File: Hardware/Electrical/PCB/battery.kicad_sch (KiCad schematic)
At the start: 0 parts

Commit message: battery charger added
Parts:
- added BT1, BT2, BT3, BT4: Li-ion 3.3Ah, symbol Device:Battery_Cell
- added C16, C18, C26: 1u, symbol Device:C_Small
- added C17: 2.2u, symbol Device:C_Small
- added C19, C20, C21: 0.1u, symbol Device:C_Small
- added C22: 22p, symbol Device:C_Small
- added C23, C24: 10u, symbol Device:C
- added C25: 100n, symbol Device:C
- added D3: BAT43W-V, Diode_SMD:D_SOD-123, symbol Diode:BAT43W-V
- added D4: SS34, Diode_SMD:D_SMC, symbol Diode:SS34
- added J2: jst, symbol Connector_Generic:Conn_01x02
- added L2: L, symbol Device:L
- added Q1, Q2: DMT6008LFG-7, Package_SON:Diodes_PowerDI3333-8, symbol Transistor_FET:DMT6008LFG
- added R10: 10m, symbol Device:R_Small
- added R11: 931k, symbol Device:R
- added R12: 133k, symbol Device:R
- added R13, R14: 10k, symbol Device:R
- added R15: 5.1k, symbol Device:R
- added R16: 430k, symbol Device:R
- added R17: 115k, symbol Device:R
- added R18: 25.5k, symbol Device:R
- added R8: 10, symbol Device:R_Small
- added R9: 2k, symbol Device:R_Small
- added U6: BQ24600, Package_DFN_QFN:Texas_RVA_VQFN-16-1EP_3.5x3.5mm_P0.5mm_EP2.14x2.14mm_ThermalVias, symbol Battery_Management:BQ24650
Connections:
- new net: BT4.1 (+), C20.2, C22.2, C23.1, C24.1, C25.1, R10.2, R11.1, U6.9 (SRN)
- new net: BT3.1 (+), BT4.2 (-)
- new net: Q1.4 (G), U6.13 (LODRV)
- new net: C19.2, L2.1, Q1.5 (D), Q2.1 (S), Q2.2 (S), Q2.3 (S), U6.14 (PH)
- new net: C20.1, C21.2, L2.2, R10.1, U6.10 (SRP)
- new net: C17.1, R9.2
- new net: BT1.1 (+), BT2.2 (-)
- new net: C22.1, R11.2, R12.1, U6.8 (VFB)
- new net: BT2.1 (+), BT3.2 (-)
- new net: C19.1, D3.1 (K), U6.16 (BTST)
- new net: C18.1, D3.2 (A), U6.12 (REGN)
- new net: C16.1, R8.2, U6.1 (VCC)
- new net: Q2.4 (G), U6.15 (HIDRV)
- new net: D4.1 (K), Q2.5 (D), R8.1
- new net +3.3V: R13.1, R14.1
- new net CHARGE_EN: U6.2 (CE)
- new net GND: BT1.2 (-), C16.2, C17.2, C18.2, C21.1, C23.2, C24.2, C25.2, C26.2, J2.2 (Pin_2), Q1.1 (S), Q1.2 (S), Q1.3 (S), R12.2, R16.2, R18.2, U6.11 (GND), U6.17 (GND)
- new net ISET_BT: R17.2, R18.1, U6.7 (ISET)
- new net PD_PWR: D4.2 (A), R9.1
- new net PG_BT: R14.2, U6.5 (PG)
- new net STATUS_BT: R13.2, U6.3 (STAT1)
- new net TEMPSNS_BT: J2.1 (Pin_1), R15.2, R16.1, U6.4 (TS)
- new net VREF_BT: C26.1, R15.1, R17.1, U6.6 (VREF)
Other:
- note added: "10k NTC"
- note added: "From USBC PD"
- note added: "To uC"
- note added: "Unclear if Working Change Values in Testing Maybe disable Later"
- note added: "VREF 2.1V VSET 4*4.2V=16.8V"
- note added: "set to 55°C"

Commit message: project state at start of school project
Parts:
- removed BT2, BT3, BT4: Li-ion 3.3Ah, symbol Device:Battery_Cell
- removed C17: 2.2u, symbol Device:C_Small
- removed C18, C26: 1u, symbol Device:C_Small
- removed C19, C20, C21: 0.1u, symbol Device:C_Small
- removed C22: 22p, symbol Device:C_Small
- removed C23, C24: 10u, symbol Device:C
- removed C25: 100n, symbol Device:C
- removed D3: BAT43W-V, Diode_SMD:D_SOD-123, symbol Diode:BAT43W-V
- removed D4: SS34, Diode_SMD:D_SMC, symbol Diode:SS34
- removed J2: jst, symbol Connector_Generic:Conn_01x02
- removed Q1, Q2: DMT6008LFG-7, Package_SON:Diodes_PowerDI3333-8, symbol Transistor_FET:DMT6008LFG
- removed R10: 10m, symbol Device:R_Small
- removed R11: 931k, symbol Device:R
- removed R12: 133k, symbol Device:R
- removed R13, R14: 10k, symbol Device:R
- removed R15: 5.1k, symbol Device:R
- removed R16: 430k, symbol Device:R
- removed R17: 115k, symbol Device:R
- removed R18: 25.5k, symbol Device:R
- removed R8: 10, symbol Device:R_Small
- removed R9: 2k, symbol Device:R_Small
- removed U6: BQ24600, Package_DFN_QFN:Texas_RVA_VQFN-16-1EP_3.5x3.5mm_P0.5mm_EP2.14x2.14mm_ThermalVias, symbol Battery_Management:BQ24650
- added U6: BQ25303JRTER, RTE0016C, symbol BQ25303JRTER:BQ25303JRTER
- BT1: value Li-ion 3.3Ah -> Battery_Cell
- C16: value 1u -> 47n
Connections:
- net GND: now also U6.11 (GND), U6.12 (GND), U6.17 (PAD), U6.5 (POL), U6.8 (NC); no longer C16.2
- net PD_PWR: now also U6.1 (VBUS), U6.6 (EN_N)
- net at L2.1: now also C16.1, U6.13 (SW), U6.14 (SW)
- net at L2.2: now also BT1.1 (+), U6.10 (BAT)
- new net: C16.2, U6.15 (BTST)
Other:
- note removed: "10k NTC"
- note removed: "From USBC PD"
- note removed: "To uC"
- note removed: "Unclear if Working Change Values in Testing Maybe disable Later"
- note removed: "VREF 2.1V VSET 4*4.2V=16.8V"
- note removed: "set to 55°C"

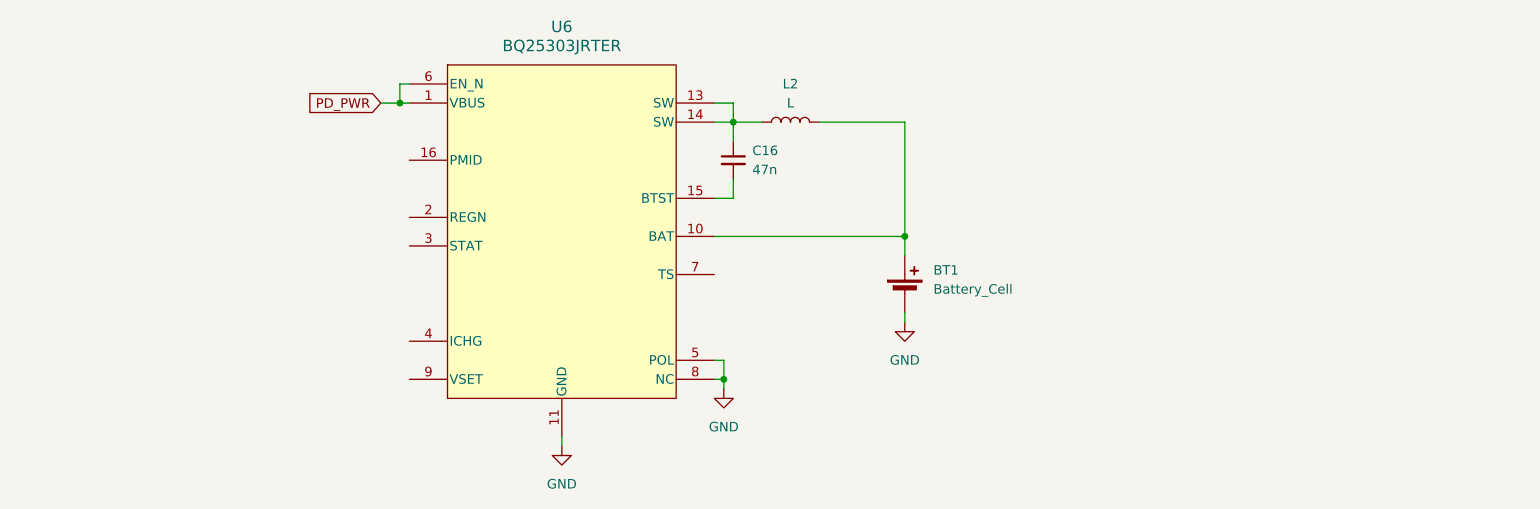
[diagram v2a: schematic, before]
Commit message: Basic Schematic finished, external connectors missing, no footprints or LCSC numbers yet
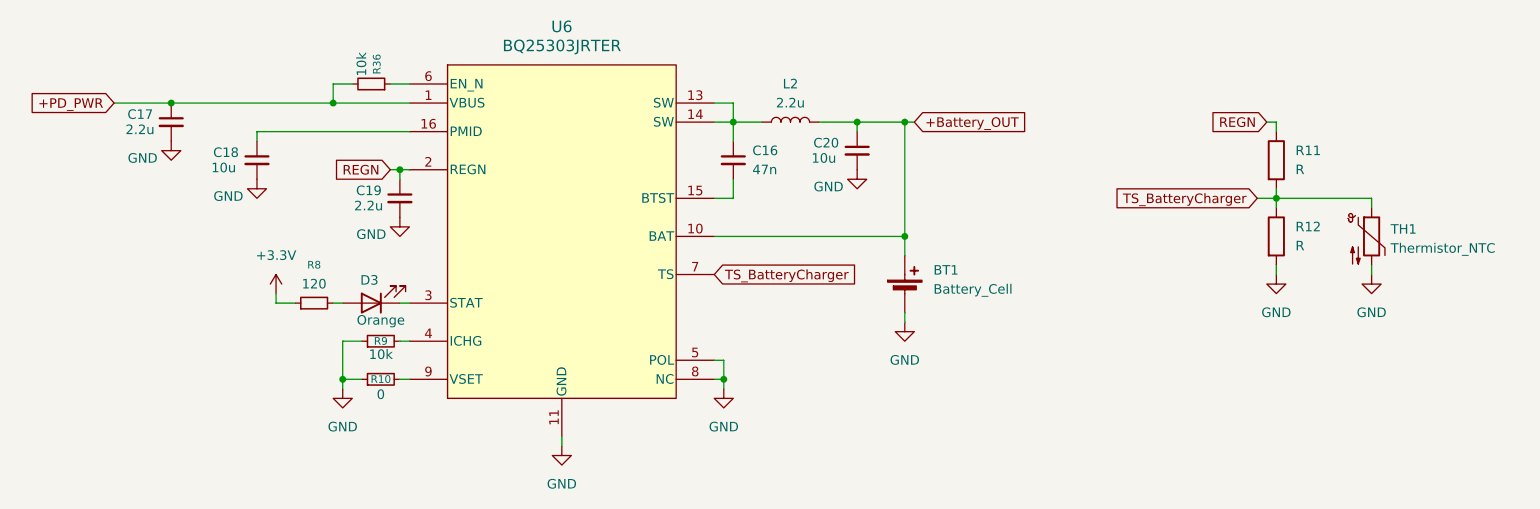
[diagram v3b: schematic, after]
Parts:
- added C17, C19: 2.2u, symbol Device:C_Small
- added C18, C20: 10u, symbol Device:C_Small
- added D3: Orange, symbol Device:LED
- added R10: 0, symbol Device:R_Small
- added R11, R12: R, symbol Device:R
- added R36, R9: 10k, symbol Device:R_Small
- added R8: 120, symbol Device:R_Small
- added TH1: Thermistor_NTC, symbol Device:Thermistor_NTC
- L2: value L -> 2.2u
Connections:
- net GND: now also C17.2, C18.2, C19.2, C20.2, R10.1, R12.2, R9.1, TH1.2
- net +Battery_OUT: now reaches BT1.1 (+), L2.2, U6.10 (BAT)
- net +Battery_OUT: now also C20.1
- net at U6.16 (PMID): now also C18.1
- net REGN: now reaches U6.2 (REGN)
- net REGN: now also C19.1, R11.1
- net at U6.3 (STAT): now also D3.1 (K)
- net at U6.4 (ICHG): now also R9.2
- net TS_BatteryCharger: now reaches U6.7 (TS)
- net TS_BatteryCharger: now also R11.2, R12.1, TH1.1
- net at U6.9 (VSET): now also R10.2
- net PD_PWR: no longer names the net of U6.6 (EN_N)
- net PD_PWR: now also R36.1; no longer U6.1 (VBUS)
- new net: D3.2 (A), R8.2
- new net +3.3V: R8.1
- new net +PD_PWR: C17.1, R36.2, U6.1 (VBUS)

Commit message: layout v1 finished but not confirmed yet
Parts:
- removed TH1: Thermistor_NTC, symbol Device:Thermistor_NTC
- added J8: 10k NTC, Connector_JST:JST_SH_BM02B-SRSS-TB_1x02-1MP_P1.00mm_Vertical, symbol Connector_Generic_MountingPin:Conn_01x02_MountingPin
- BT1: footprint (none) -> Connector_Molex:Molex_Micro-Fit_3.0_43650-0224_1x02-1MP_P3.00mm_Vertical; symbol Device:Battery_Cell -> Connector_Generic_MountingPin:Conn_01x02_MountingPin; *LCSC Part Number (none) -> C122425
- C16: footprint (none) -> Capacitor_SMD:C_0603_1608Metric; *LCSC Part Number (none) -> C1622
- C17, C19: footprint (none) -> Capacitor_SMD:C_0603_1608Metric; *LCSC Part Number (none) -> C23630
- C18, C20: footprint (none) -> Capacitor_SMD:C_1206_3216Metric; *LCSC Part Number (none) -> C13585
- D3: footprint (none) -> LED_SMD:LED_0603_1608Metric; *LCSC Part Number (none) -> C2286
- L2: footprint (none) -> Inductor_SMD:L_Bourns_SRP5030T; *LCSC Part Number (none) -> C2847475
- R10, R8: footprint (none) -> Resistor_SMD:R_0603_1608Metric; *LCSC Part Number (none) -> C21189
- R11: value R -> 4.32k; footprint (none) -> Resistor_SMD:R_0603_1608Metric; *LCSC Part Number (none) -> C23158
- R12: value R -> 21k; footprint (none) -> Resistor_SMD:R_0603_1608Metric; *LCSC Part Number (none) -> C137769
- R36, R9: footprint (none) -> Resistor_SMD:R_0603_1608Metric; *LCSC Part Number (none) -> C25804
- U6: footprint RTE0016C -> Package_DFN_QFN:WQFN-16-1EP_3x3mm_P0.5mm_EP1.68x1.68mm; *LCSC Part Number (none) -> C2842775
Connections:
- net GND: now also J8.2 (Pin_2)
- net TS_BatteryCharger: now also J8.1 (Pin_1)
- net EN_BAT: now reaches R36.1, U6.6 (EN_N)
- no-connect marks 0 -> 2
